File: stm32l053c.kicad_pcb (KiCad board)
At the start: 2 copper layers, 20.8 x 43.7 mm, 21 parts, among them P1 SWD, P2 CONN_01X17, P3 CONN_01X17, P4 Ext Xtal, U1 STM32L053C8_LQFP48

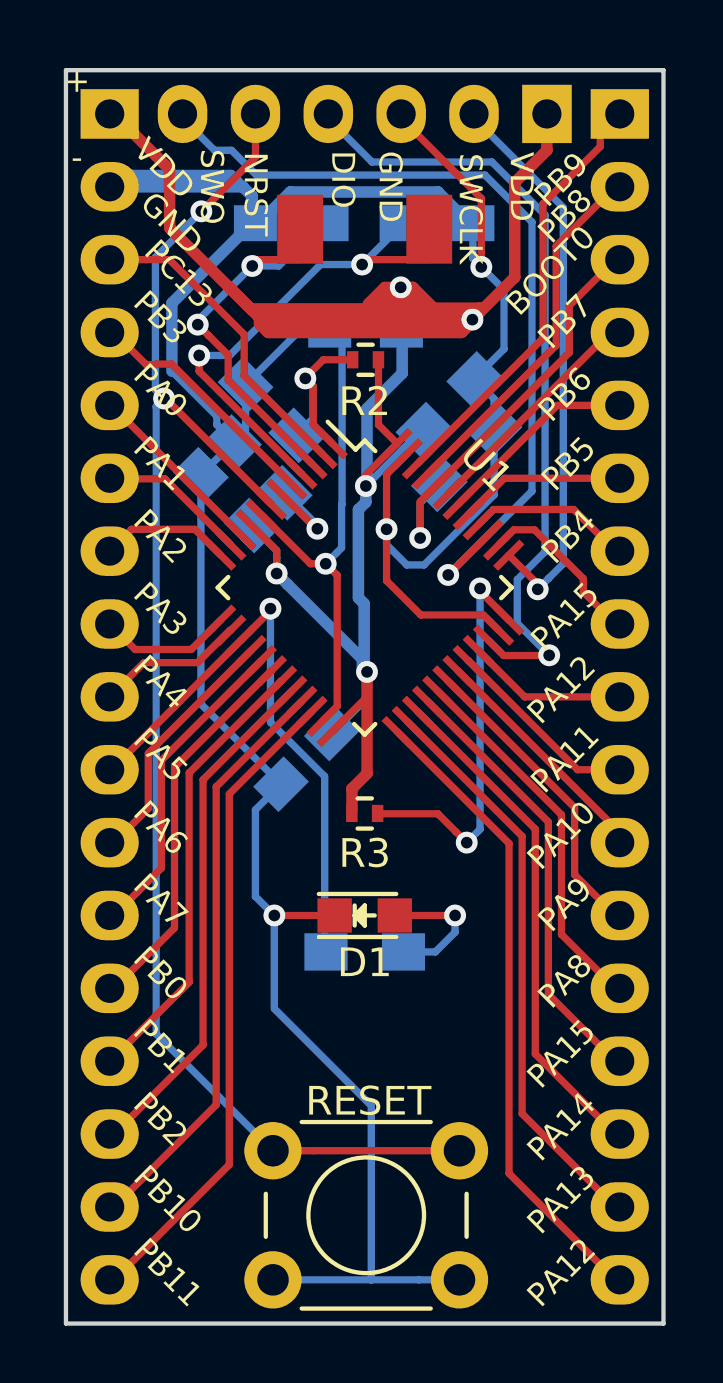
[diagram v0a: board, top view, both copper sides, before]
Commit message: Soldermask clearance
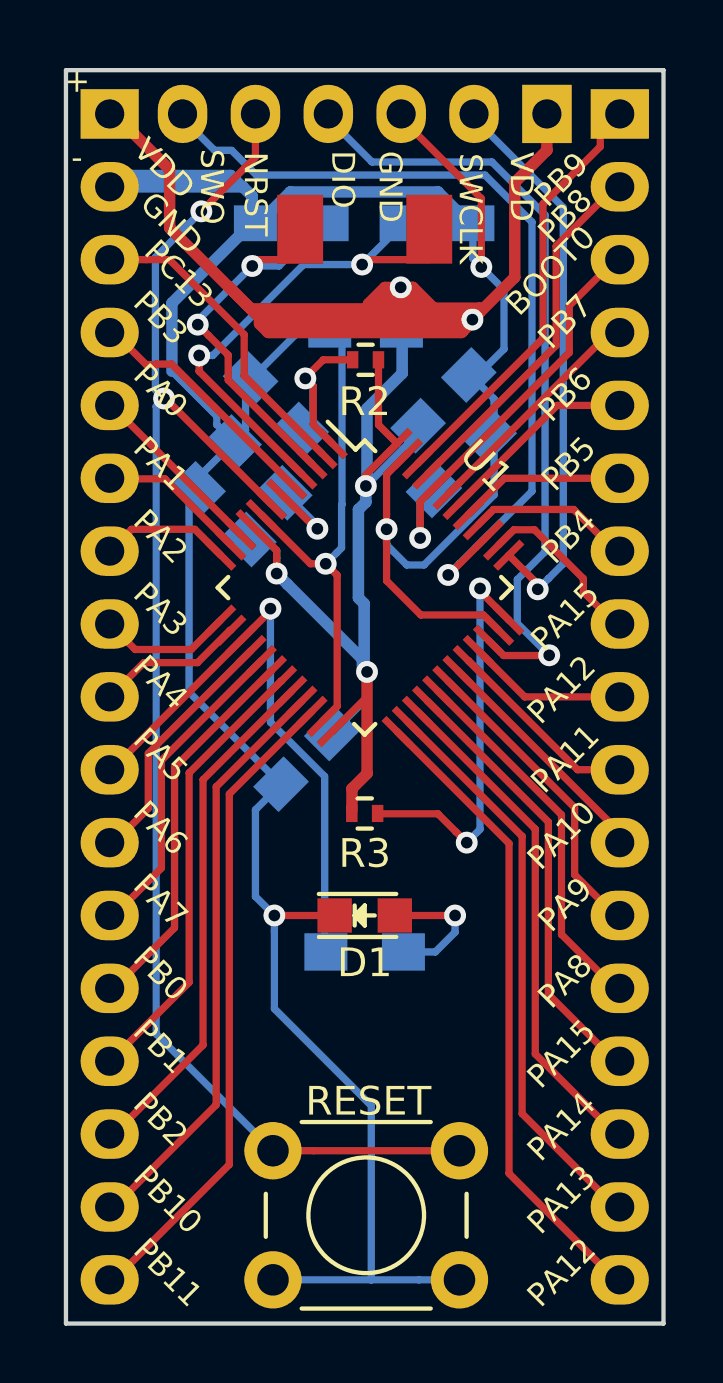
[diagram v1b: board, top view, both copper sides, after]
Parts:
- moved C8 0.50 mm to (186.8, 95.2)
- moved R1 0.28 mm to (195.1, 93.4)
- moved C4 0.27 mm to (188.7, 91.4)
- moved C7 0.23 mm to (194.5, 91.3)
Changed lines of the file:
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@@
   (page A4)
   (layers
-    (0 F.Cu signal hide)
-    (31 B.Cu signal hide)
+    (0 F.Cu signal)
+    (31 B.Cu signal)
     (32 B.Adhes user)
     (33 F.Adhes user)
@@
     (pad_to_mask_clearance 0.2)
     (aux_axis_origin 0 0)
-    (visible_elements FFFEF37F)
+    (visible_elements FFFEF77F)
     (pcbplotparams
       (layerselection 0x010f0_80000001)
@@
   )
   (module Capacitors_SMD:C_0805_HandSoldering (layer B.Cu)
-    (at 188.5 91.6 315)
+    (at 188.676317 91.394317 315)
     (descr "Capacitor SMD 0805, hand soldering")
     (tags "capacitor 0805")
@@
   )
   (module Resistors_SMD:R_0805_HandSoldering (layer B.Cu)
-    (at 195.326 93.218 45)
+    (at 195.137594 93.431806 45)
     (descr "Resistor SMD 0805, hand soldering")
     (tags "resistor 0805")
@@
   )
   (module Capacitors_SMD:C_0805_HandSoldering (layer B.Cu)
-    (at 194.7 91.4 45)
+    (at 194.5132 91.2622 45)
     (descr "Capacitor SMD 0805, hand soldering")
     (tags "capacitor 0805")
@@
   )
   (module Capacitors_SMD:C_0805_HandSoldering (layer B.Cu)
-    (at 186.944 94.742 135)
+    (at 186.847517 95.229717 135)
     (descr "Capacitor SMD 0805, hand soldering")
     (tags "capacitor 0805")
@@
   (via (at 191.81 94.25) (size 0.762) (drill 0.4064) (layers F.Cu B.Cu) (net 1))
   (segment (start 193.816117 92.283883) (end 193.106117 92.283883) (width 0.254) (layer B.Cu) (net 1))
+  (segment (start 187.216117 92.716117) (end 187.202117 92.716117) (width 0.254) (layer B.Cu) (net 2))
+  (segment (start 187.202117 92.716117) (end 185.6486 94.269634) (width 0.254) (layer B.Cu) (net 2))
+  (segment (start 185.6486 101.437366) (end 188.854117 104.642883) (width 0.254) (layer B.Cu) (net 2))
+  (segment (start 185.6486 94.269634) (end 185.6486 101.437366) (width 0.254) (layer B.Cu) (net 2))
   (segment (start 188.854117 104.642883) (end 187.96 105.537) (width 0.254) (layer B.Cu) (net 2))
   (segment (start 187.96 105.537) (end 187.96 108.5596) (width 0.254) (layer B.Cu) (net 2))
@@
   (segment (start 192 121.92) (end 188.572 121.92) (width 0.254) (layer B.Cu) (net 2))
   (segment (start 195.072 121.92) (end 193.657787 121.92) (width 0.254) (layer B.Cu) (net 2))
-  (segment (start 186.060117 93.858117) (end 186.060117 101.848883) (width 0.254) (layer B.Cu) (net 2))
-  (segment (start 186.060117 101.848883) (end 188.854117 104.642883) (width 0.254) (layer B.Cu) (net 2))
-  (segment (start 187.216117 92.716117) (end 187.202117 92.716117) (width 0.254) (layer B.Cu) (net 2))
-  (segment (start 187.202117 92.716117) (end 186.060117 93.858117) (width 0.254) (layer B.Cu) (net 2))
   (segment (start 187.616117 90.716117) (end 187.616117 92.316117) (width 0.254) (layer B.Cu) (net 2))
   (segment (start 187.616117 92.316117) (end 187.216117 92.716117) (width 0.254) (layer B.Cu) (net 2))
@@
   (segment (start 198.9 87.9676) (end 200.5076 86.36) (width 0.254) (layer F.Cu) (net 37))
   (segment (start 200.5076 86.36) (end 200.66 86.36) (width 0.254) (layer F.Cu) (net 37))
+  (segment (start 190.46 85.09) (end 190.335 85.09) (width 0.254) (layer B.Cu) (net 38))
+  (segment (start 190.335 85.09) (end 190.3222 85.0772) (width 0.254) (layer B.Cu) (net 38))
+  (segment (start 190.3222 85.0772) (end 190.3222 85.0392) (width 0.254) (layer B.Cu) (net 38))
+  (segment (start 190.3222 85.0392) (end 188.7814 86.58) (width 0.254) (layer B.Cu) (net 38))
+  (segment (start 188.7814 86.58) (end 187.85 86.58) (width 0.254) (layer B.Cu) (net 38))
   (segment (start 186.330999 89.005999) (end 185.95 88.625) (width 0.254) (layer F.Cu) (net 38))
   (segment (start 187.011202 89.686202) (end 186.330999 89.005999) (width 0.254) (layer F.Cu) (net 38))
@@
   (segment (start 187.85 86.58) (end 185.95 88.48) (width 0.254) (layer B.Cu) (net 38))
   (via (at 185.95 88.625) (size 0.762) (drill 0.4064) (layers F.Cu B.Cu) (net 38))
-  (segment (start 189.3 86.125) (end 189.225 86.125) (width 0.254) (layer B.Cu) (net 38))
-  (segment (start 190.335 85.09) (end 189.3 86.125) (width 0.254) (layer B.Cu) (net 38))
-  (segment (start 189.225 86.125) (end 188.77 86.58) (width 0.254) (layer B.Cu) (net 38))
-  (segment (start 190.46 85.09) (end 190.335 85.09) (width 0.254) (layer B.Cu) (net 38))
-  (segment (start 188.77 86.58) (end 187.85 86.58) (width 0.254) (layer B.Cu) (net 38))
   (via (at 187.85 86.58) (size 0.762) (drill 0.4064) (layers F.Cu B.Cu) (net 38))
   (segment (start 188.07 86.36) (end 187.85 86.58) (width 0.254) (layer F.Cu) (net 38))
   (segment (start 189.51956 86.36) (end 188.07 86.36) (width 0.254) (layer F.Cu) (net 38))
+  (segment (start 186 89.7) (end 186.4742 89.7) (width 0.254) (layer B.Cu) (net 39))
+  (segment (start 186.4742 89.7) (end 189.6442 86.53) (width 0.254) (layer B.Cu) (net 39))
+  (segment (start 189.6442 86.53) (end 191.141185 86.53) (width 0.254) (layer B.Cu) (net 39))
   (segment (start 191.141185 86.53) (end 191.68 86.53) (width 0.254) (layer B.Cu) (net 39))
-  (segment (start 190.23 86.53) (end 191.141185 86.53) (width 0.254) (layer B.Cu) (net 39))
-  (segment (start 186 89.7) (end 187.06 89.7) (width 0.254) (layer B.Cu) (net 39))
-  (segment (start 187.06 89.7) (end 190.23 86.53) (width 0.254) (layer B.Cu) (net 39))
   (segment (start 193.04 85.09) (end 193.04 85.17) (width 0.254) (layer B.Cu) (net 39))
   (segment (start 193.04 85.17) (end 191.68 86.53) (width 0.254) (layer B.Cu) (net 39))

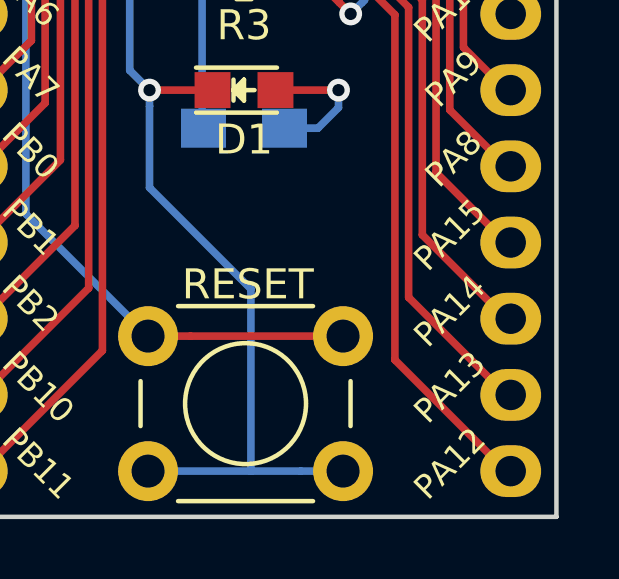
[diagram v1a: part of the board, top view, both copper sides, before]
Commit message: Correctd labels for PB12 to PB15
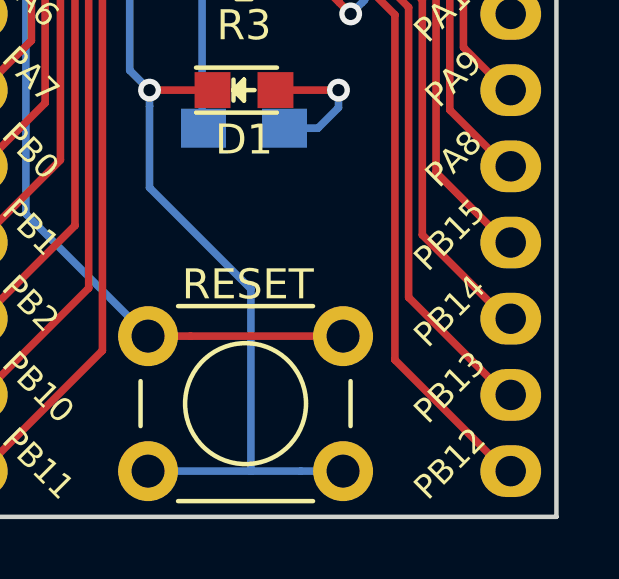
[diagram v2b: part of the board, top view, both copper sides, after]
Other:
- board text added: "PB12"
- board text added: "PB13"
- board text added: "PB14"
- board text added: "PB15"
- board text removed: "PA13"
- board text removed: "PA14"
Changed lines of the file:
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@@
   (page A4)
   (layers
-    (0 F.Cu signal)
-    (31 B.Cu signal)
+    (0 F.Cu signal hide)
+    (31 B.Cu signal hide)
     (32 B.Adhes user)
     (33 F.Adhes user)
     (34 B.Paste user)
     (35 F.Paste user)
-    (36 B.SilkS user)
+    (36 B.SilkS user hide)
     (37 F.SilkS user)
     (38 B.Mask user)
@@
     (effects (font (size 0.8 0.8) (thickness 0.15)) (justify mirror))
   )
-  (gr_text PA12 (at 198.628 121.666 45) (layer F.SilkS)
+  (gr_text PB12 (at 198.628 121.666 45) (layer F.SilkS)
     (effects (font (size 0.8 0.8) (thickness 0.15)))
   )
-  (gr_text PA13 (at 198.628 119.126 45) (layer F.SilkS)
+  (gr_text PB13 (at 198.628 119.126 45) (layer F.SilkS)
     (effects (font (size 0.8 0.8) (thickness 0.15)))
   )
-  (gr_text PA14 (at 198.628 116.586 45) (layer F.SilkS)
+  (gr_text PB14 (at 198.628 116.586 45) (layer F.SilkS)
     (effects (font (size 0.8 0.8) (thickness 0.15)))
   )
-  (gr_text PA15 (at 198.628 114.046 45) (layer F.SilkS)
+  (gr_text PB15 (at 198.628 114.046 45) (layer F.SilkS)
     (effects (font (size 0.8 0.8) (thickness 0.15)))
   )
